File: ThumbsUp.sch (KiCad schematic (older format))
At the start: 152 parts, among them IC1 RP2040, IC2 W25Q128JVSIM, IC3 RP2040, IC4 W25Q128JVSIM, J1 Conn_01x04_Male, J10 Raiser_Male, J11 Raiser_Female, J12 Raiser_Male, J13 Raiser_Female, J14 Raiser_Male, J15 Raiser_Female, J16 Raiser_Male, J17 Raiser_Female, J18 Raiser_Male, J19 Raiser_Female, J2 Conn_01x04_Male, J20 Conn_01x04_Female, J21 Conn_01x04_Female, J22 Conn_01x04_Female, J23 Conn_01x04_Female, J24 Conn_01x04_Male, J25 Conn_01x04_Male, J26 Conn_01x04_Male, J27 Conn_01x04_Male, J28 Conn_01x04_Female, J29 Conn_01x04_Female, J3 Conn_01x04_Female, J30 Conn_01x04_Female, J31 Conn_01x04_Female, J32 USB_C_Receptacle_USB2.0, J33 Raiser_Male, J34 Raiser_Female, J35 Raiser_Male, J36 STX-3501-3N, J37 USB_C_Receptacle_USB2.0, J38 Raiser_Female, J39 Raiser_Male, J4 Conn_01x04_Male, J40 Raiser_Female, J41 Raiser_Male, J42 Raiser_Female, J43 Raiser_Male, J44 Raiser_Female, J45 Raiser_Male, J46 STX-3501-3N, J47 Raiser_Female, J48 Raiser_Male, J5 Conn_01x04_Female, J6 Conn_01x04_Male, J7 Conn_01x04_Male, J8 Conn_01x04_Male, J9 Raiser_Female, U1 NCP1117-3.3_SOT223, U2 NCP1117-3.3_SOT223, Y1 ABLS-12.000MHZ-B4-T, Y2 ABLS-12.000MHZ-B4-T

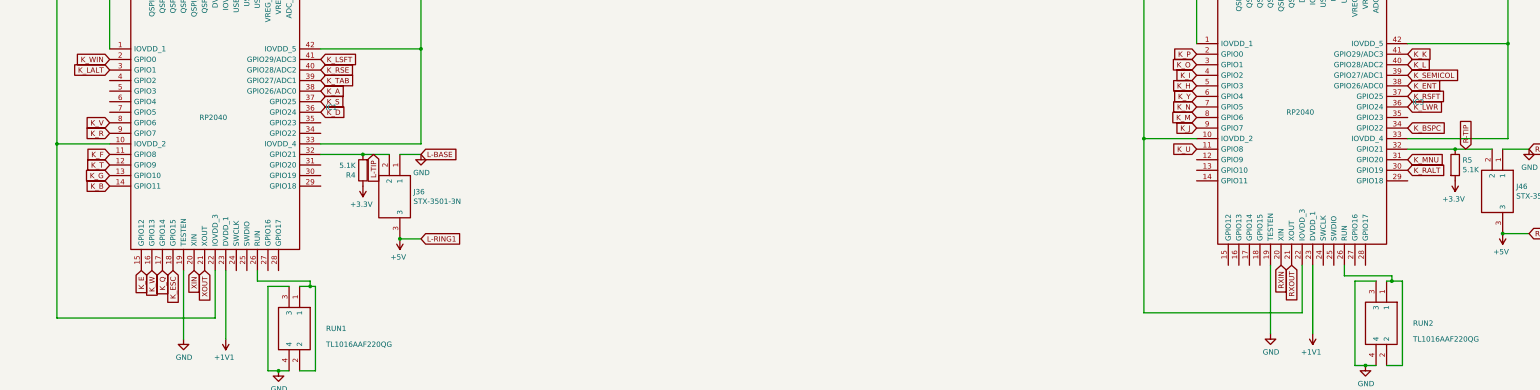
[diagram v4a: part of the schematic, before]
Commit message: Fixed the missing connectors and handiness pins
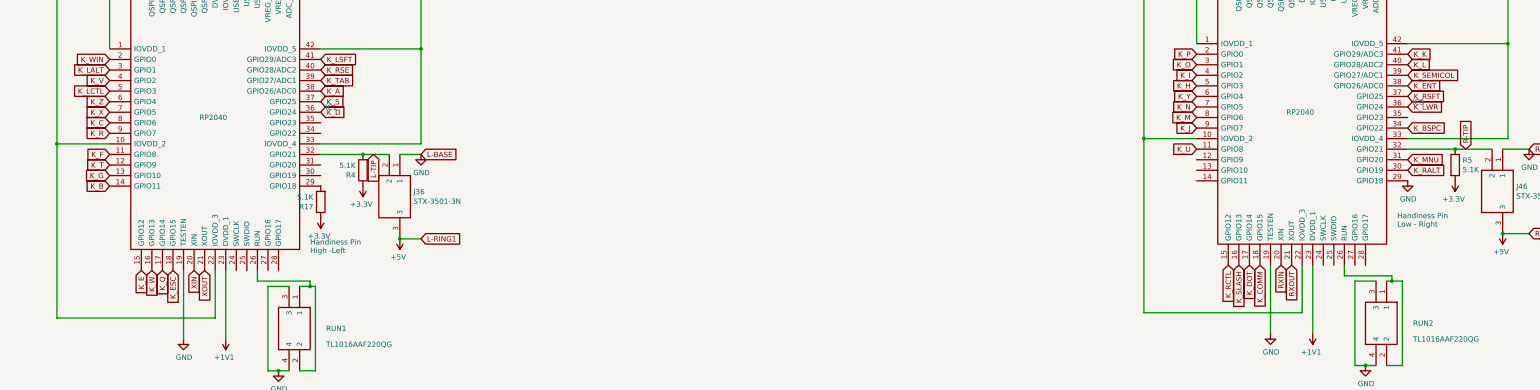
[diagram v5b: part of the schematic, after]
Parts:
- added R17: 5.1K, Resistor_SMD:R_0402_1005Metric, symbol Device:R
- R4, R5: footprint Resistor_SMD:R_0805_2012Metric -> Resistor_SMD:R_0402_1005Metric
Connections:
- net +3V3: now also R17.1
- net GND: now also IC3.29 (GPIO18)
- net K_C: now also IC1.8 (GPIO6)
- net K_COMM: now also IC3.18 (GPIO15)
- net K_DOT: now also IC3.17 (GPIO14)
- net K_LCTL: now also IC1.5 (GPIO3)
- net K_RCTL: now also IC3.15 (GPIO12)
- net K_SLASH: now also IC3.16 (GPIO13)
- net K_V: now also IC1.4 (GPIO2); no longer IC1.8 (GPIO6)
- net K_X: now also IC1.7 (GPIO5)
- net K_Z: now also IC1.6 (GPIO4)
- net at IC1.29 (GPIO18): now also R17.2
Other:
- note added: "Handiness Pin\nHigh -Left"
- note added: "Handiness Pin\nLow - Right"
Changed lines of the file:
@@
 F 0 "R4" H 4720 8296 50  0000 L CNN
 F 1 "5.1K" H 4720 8205 50  0000 L CNN
-F 2 "Resistor_SMD:R_0805_2012Metric" V 4580 8250 50  0001 C CNN
+F 2 "Resistor_SMD:R_0402_1005Metric" V 4580 8250 50  0001 C CNN
 F 3 "~" H 4650 8250 50  0001 C CNN
 	1    4650 8250
@@
 F 0 "R5" H 15070 8246 50  0000 L CNN
 F 1 "5.1K" H 15070 8155 50  0000 L CNN
-F 2 "Resistor_SMD:R_0805_2012Metric" V 14930 8200 50  0001 C CNN
+F 2 "Resistor_SMD:R_0402_1005Metric" V 14930 8200 50  0001 C CNN
 F 3 "~" H 15000 8200 50  0001 C CNN
 	1    15000 8200
@@
 Text GLabel 2250 7900 0    50   Input ~ 0
 K_R
-Text GLabel 2250 7800 0    50   Input ~ 0
+Text GLabel 2250 7400 0    50   Input ~ 0
 K_V
 Wire Wire Line
@@
 Text GLabel 13100 3800 0    50   Input ~ 0
 RQSPI_SSN
+Text GLabel 12850 9150 3    50   Input ~ 0
+K_RCTL
+Text GLabel 12950 9150 3    50   Input ~ 0
+K_SLASH
+Text GLabel 13050 9150 3    50   Input ~ 0
+K_DOT
+Text GLabel 13150 9150 3    50   Input ~ 0
+K_COMM
+Text GLabel 2250 7500 0    50   Input ~ 0
+K_LCTL
+Text GLabel 2250 7600 0    50   Input ~ 0
+K_Z
+Text GLabel 2250 7700 0    50   Input ~ 0
+K_X
+Text GLabel 2250 7800 0    50   Input ~ 0
+K_C
+$Comp
+L Device:R R17
+U 1 1 63DB25AE
+P 4250 8550
+F 0 "R17" H 4320 8596 50  0000 L CNN
+F 1 "5.1K" H 4320 8505 50  0000 L CNN
+F 2 "Resistor_SMD:R_0402_1005Metric" V 4180 8550 50  0001 C CNN
+F 3 "~" H 4250 8550 50  0001 C CNN
+	1    4250 8550
+	-1   0    0    1
+$EndComp
+$Comp
+L power:+3.3V #PWR0157
+U 1 1 63DB2E0C
+P 4250 8700
+F 0 "#PWR0157" H 4250 8550 50  0001 C CNN
+F 1 "+3.3V" H 4265 8873 50  0000 C CNN
+F 2 "" H 4250 8700 50  0001 C CNN
+F 3 "" H 4250 8700 50  0001 C CNN
+	1    4250 8700
+	-1   0    0    1
+$EndComp
+Text Notes 4150 9050 0    50   ~ 0
+Handiness Pin\nHigh -Left
+Text Notes 14450 8800 0    50   ~ 0
+Handiness Pin\nLow - Right
+$Comp
+L power:GND #PWR0158
+U 1 1 63DB80C5
+P 14550 8350
+F 0 "#PWR0158" H 14550 8100 50  0001 C CNN
+F 1 "GND" H 14555 8177 50  0000 C CNN
+F 2 "" H 14550 8350 50  0001 C CNN
+F 3 "" H 14550 8350 50  0001 C CNN
+	1    14550 8350
+	1    0    0    -1
+$EndComp
 $EndSCHEMATC
